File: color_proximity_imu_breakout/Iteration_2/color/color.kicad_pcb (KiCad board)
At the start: 2 copper layers, 15 x 16.5 mm, 10 parts, among them J4 Conn_01x05, U6 ICM-20602

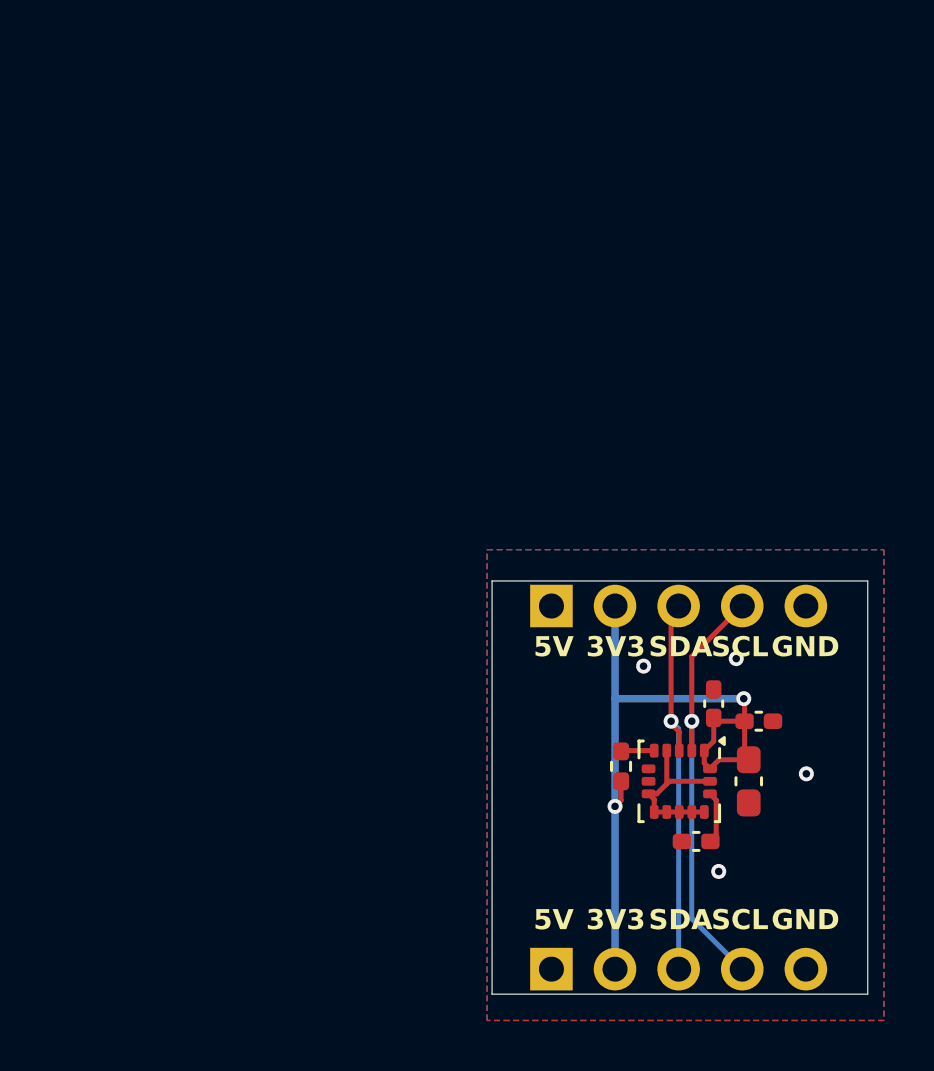
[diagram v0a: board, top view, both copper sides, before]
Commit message: Iteration 2 of color, distance, and imu sensor boards
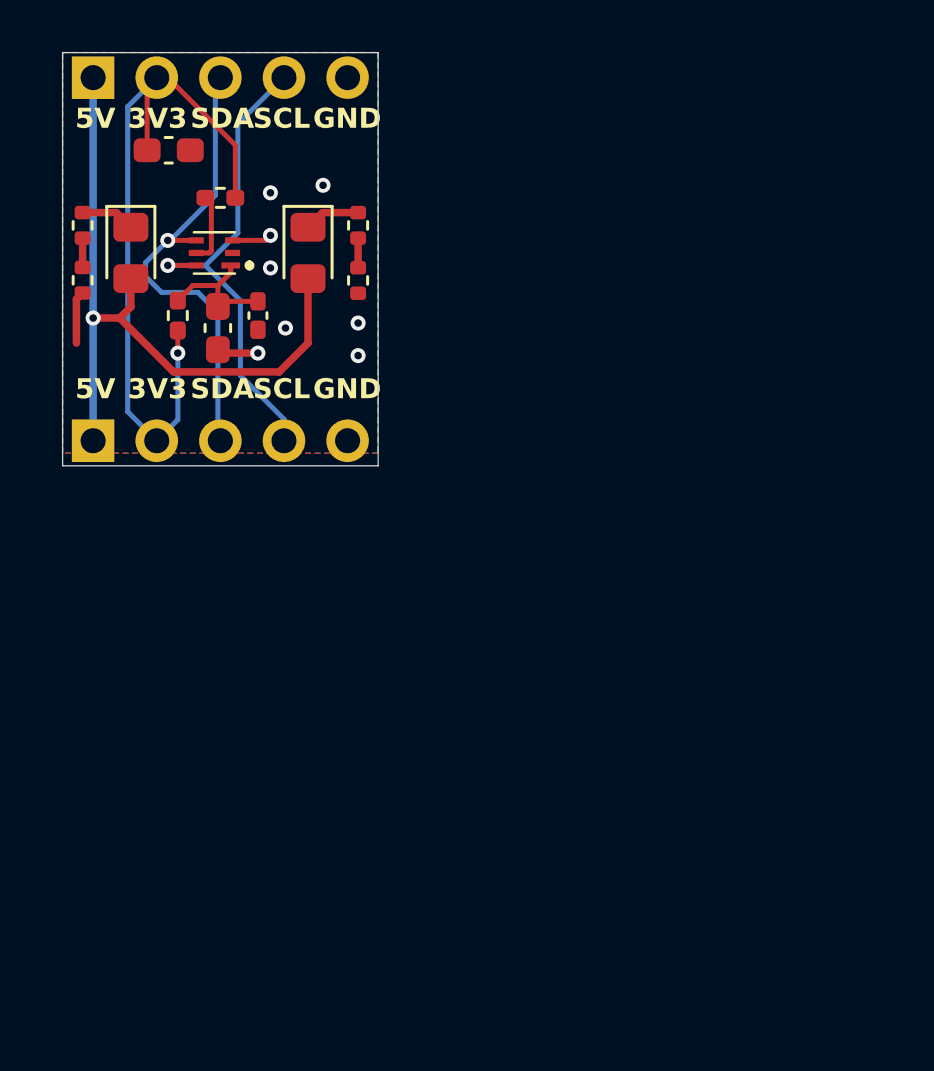
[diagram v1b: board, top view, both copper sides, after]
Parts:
- removed C10, C7: 0.1u, Capacitor_SMD:C_0402_1005Metric_Pad0.74x0.62mm_HandSolder
- removed C8: 2.2u, Capacitor_SMD:C_0603_1608Metric_Pad1.08x0.95mm_HandSolder
- removed C9: 10n, Capacitor_SMD:C_0402_1005Metric_Pad0.74x0.62mm_HandSolder
- removed the G*** at (122.8, 129.5)
- removed the G*** at (124.4, 134.3)
- removed the J4 at (121.4, 140.7)
- removed the J4 at (121.4, 126.2)
- removed R19: 4.7k, Resistor_SMD:R_0402_1005Metric_Pad0.72x0.64mm_HandSolder
- removed U6: ICM-20602, Package_LGA:LGA-16_3x3mm_P0.5mm_LayoutBorder3x5y
- added C14: 10u, Capacitor_SMD:C_0603_1608Metric_Pad1.08x0.95mm_HandSolder, F.Cu at (106.1, 108.0)
- added C4: 1u, Capacitor_SMD:C_0603_1608Metric_Pad1.08x0.95mm_HandSolder, F.Cu at (108.1, 115.1)
- added C5: 0.1u, Capacitor_SMD:C_0402_1005Metric_Pad0.74x0.62mm_HandSolder, F.Cu at (109.7, 114.6)
- added D1: WHITE, LED_SMD:LED_0805_2012Metric_Pad1.15x1.40mm_HandSolder, F.Cu at (111.7, 112.1)
- added D2: WHITE, LED_SMD:LED_0805_2012Metric_Pad1.15x1.40mm_HandSolder, F.Cu at (104.6, 112.1)
- added G***: LOGO, LOGO, B.Cu at (104.5, 108.4)
- added G***: LOGO, LOGO, B.Cu at (105.2, 113.5)
- added IC2: ISL29125IROZ-T7, ISL29125:ISL29125IROZT7, F.Cu at (108.0, 112.1)
- added J4: Conn_01x05, Connector_PinHeader_2.54mm:PinHeader_1x05_P2.54mm_Vertical, F.Cu at (103.1, 105.1)
- added J4: Conn_01x05, Connector_PinHeader_2.54mm:PinHeader_1x05_P2.54mm_Vertical, F.Cu at (103.1, 119.6)
- added R15: 100, Resistor_SMD:R_0402_1005Metric_Pad0.72x0.64mm_HandSolder, F.Cu at (106.5, 114.6)
- added R16: 4.7k, Resistor_SMD:R_0402_1005Metric_Pad0.72x0.64mm_HandSolder, F.Cu at (108.2, 109.9)
- added R17: 120, Resistor_SMD:R_0402_1005Metric, F.Cu at (113.7, 111.0)
- added R18: 120, Resistor_SMD:R_0402_1005Metric, F.Cu at (102.7, 111.0)
- added R30: 120, Resistor_SMD:R_0402_1005Metric, F.Cu at (113.7, 113.2)
- added R32: 120, Resistor_SMD:R_0402_1005Metric, F.Cu at (102.7, 113.2)
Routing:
- net +5V: track 0.02 -> 28.8 mm, vias 0 -> 1
- net Net-(IC2-VDD): track 0.00 -> 5.39 mm
- net Net-(IC2-~{INT}): track 0.00 -> 2.86 mm
- net /sda: track 16.3 -> 19.1 mm
- net Net-(D2-K): track 0.00 -> 2.62 mm
- net Net-(D1-K): track 0.00 -> 2.57 mm
- net /scl: track 17.3 -> 19.7 mm
- net Net-(U6-REGOUT): track 2.10 -> 0.00 mm
- net Net-(U6-~{CS}): track 1.34 -> 0.00 mm
- net GND: track 6.80 -> 5.49 mm, vias 4 -> 8
- net Net-(R17-Pad2): track 0.00 -> 1.18 mm
- net Net-(R18-Pad2): track 0.00 -> 1.17 mm
- net +3.3V: track 29.0 -> 29.6 mm, vias 2 -> 1
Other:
- board size 15 x 16.5 mm -> 12.6 x 16.5 mm

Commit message: Color Board Iteration 2 Updated
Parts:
- removed J4 (x2): Conn_01x05, Connector_PinHeader_2.54mm:PinHeader_1x05_P2.54mm_Vertical
- added C1: 10u, Capacitor_SMD:C_0603_1608Metric_Pad1.08x0.95mm_HandSolder, F.Cu at (107.6, 116.4)
- added G***: LOGO, pcb_footprints:ras, B.Cu at (105.2, 121.6)
- added G***: LOGO, pcb_footprints:vexu_ghost, B.Cu at (112.0, 115.0)
- added J1: Conn_01x10, pcb_footprints:GT-B0502MSV27-10S1101, F.Cu at (111.6, 107.8)
- added J2: Conn_01x10, pcb_footprints:GT-B0502MSV27-10S1101, F.Cu at (105.2, 120.5)
- added REF**: MountingHole_#4_3.175mm, pcb_footprints:MountingHole_#4_3.175mm, F.Cu at (111.6, 120.5)
- added REF**: MountingHole_#4_3.175mm, pcb_footprints:MountingHole_#4_3.175mm, F.Cu at (105.2, 107.8)
- moved R18 12.5 mm to (114.2, 115.7)
- moved R17 12.1 mm to (102.5, 115.5)
- moved R32 11.8 mm to (113.8, 117.2), turned to 180 degrees
- moved R30 11.4 mm to (103.0, 117.0), turned to 0 degrees
- moved D2 8.88 mm to (113.5, 112.5), turned to 90 degrees
- moved D1 8.71 mm to (103.0, 112.5), turned to 90 degrees
- moved C14 5.85 mm to (105.4, 113.8), turned to -90 degrees
- moved R15 5.43 mm to (111.8, 113.2), turned to 90 degrees
- moved R16 3.94 mm to (110.5, 113.1), turned to -90 degrees
- moved G*** 3.82 mm to (104.9, 112.2)
- moved G*** 3.53 mm to (105.6, 117.0)
- moved C5 2.69 mm to (112.0, 116.0)
- moved C4 2.66 mm to (110.5, 116.2)
- moved IC2 1.80 mm to (108.0, 113.9), turned to 0 degrees
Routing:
- net GND: track 5.49 -> 25.9 mm, vias 8 -> 6
- net Net-(IC2-VDD): track 5.39 -> 12.3 mm, vias 0 -> 2
- net +3.3V: track 29.6 -> 34.5 mm, vias 1 -> 2
- net +5V: track 28.8 -> 25.2 mm, vias 1 -> 2
- net /sda: track 19.1 -> 20.3 mm, vias 1 -> 3
- net /scl: track 19.7 -> 18.6 mm, vias 1 -> 2
- net Net-(IC2-~{INT}): track 2.86 -> 1.86 mm
- net Net-(D1-K): track 2.57 -> 1.67 mm
- net Net-(D2-K): track 2.62 -> 2.02 mm
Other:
- board size 12.6 x 16.5 mm -> 13 x 20 mm
- board text added: "Designed By Gengwen Li Trung Le"
- board text added: "Short = increase brightness"
- board text removed: "3V3"
- board text removed: "5V"
- board text removed: "Designed By Gengwen Li"
- board text removed: "GND"
- board text removed: "SCL"
- board text removed: "SDA"

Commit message: color board iteration 2 updated
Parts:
- removed C14: 10u, Capacitor_SMD:C_0603_1608Metric_Pad1.08x0.95mm_HandSolder
- added C2: 10u, Capacitor_SMD:C_0603_1608Metric_Pad1.08x0.95mm_HandSolder, F.Cu at (105.4, 113.6)
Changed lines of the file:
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@@
 			(unlocked yes)
 			(layer "F.SilkS")
+			(hide yes)
 			(effects
 				(font
@@
 		)
 	)
+	(footprint "Capacitor_SMD:C_0603_1608Metric_Pad1.08x0.95mm_HandSolder"
+		(layer "F.Cu")
+		(at 105.4 113.6 90)
+		(descr "Capacitor SMD 0603 (1608 Metric), square (rectangular) end terminal, IPC-7351 nominal with elongated pad for handsoldering. (Body size source: IPC-SM-782 page 76, https://www.pcb-3d.com/wordpress/wp-content/uploads/ipc-sm-782a_amendment_1_and_2.pdf), generated with kicad-footprint-generator")
+		(tags "capacitor handsolder")
+		(property "Reference" "C2"
+			(at 0 -1.43 90)
+			(layer "F.SilkS")
+			(hide yes)
+			(effects
+				(font
+					(size 1 1)
+					(thickness 0.15)
+				)
+			)
+		)
+		(property "Value" "10u"
+			(at 0 1.43 90)
+			(layer "F.Fab")
+			(hide yes)
+			(effects
+				(font
+					(size 1 1)
+					(thickness 0.15)
+				)
+			)
+		)
+		(property "Datasheet" "~"
+			(at 0 0 90)
+			(layer "F.Fab")
+			(hide yes)
+			(effects
+				(font
+					(size 1.27 1.27)
+					(thickness 0.15)
+				)
+			)
+		)
+		(property "Description" "Unpolarized capacitor"
+			(at 0 0 90)
+			(layer "F.Fab")
+			(hide yes)
+			(effects
+				(font
+					(size 1.27 1.27)
+					(thickness 0.15)
+				)
+			)
+		)
+		(property "Supplier Name" "JLCPCB"
+			(at 0 0 90)
+			(unlocked yes)
+			(layer "F.Fab")
+			(hide yes)
+			(effects
+				(font
+					(size 1 1)
+					(thickness 0.15)
+				)
+			)
+		)
+		(property "Supplier Part Number" "C15849"
+			(at 0 0 90)
+			(unlocked yes)
+			(layer "F.Fab")
+			(hide yes)
+			(effects
+				(font
+					(size 1 1)
+					(thickness 0.15)
+				)
+			)
+		)
+		(property "Substitution_Value" ""
+			(at 0 0 90)
+			(unlocked yes)
+			(layer "F.Fab")
+			(hide yes)
+			(effects
+				(font
+					(size 1 1)
+					(thickness 0.15)
+				)
+			)
+		)
+		(property "Variant" ""
+			(at 0 0 90)
+			(unlocked yes)
+			(layer "F.Fab")
+			(hide yes)
+			(effects
+				(font
+					(size 1 1)
+					(thickness 0.15)
+				)
+			)
+		)
+		(property "JLCPCB Part" "C15849"
+			(at 0 0 90)
+			(unlocked yes)
+			(layer "F.Fab")
+			(hide yes)
+			(effects
+				(font
+					(size 1 1)
+					(thickness 0.15)
+				)
+			)
+		)
+		(property ki_fp_filters "C_*")
+		(sheetname "/")
+		(sheetfile "color.kicad_sch")
+		(attr smd)
+		(fp_line
+			(start -0.146267 -0.51)
+			(end 0.146267 -0.51)
+			(stroke
+				(width 0.12)
+				(type solid)
+			)
+			(layer "F.SilkS")
+		)
+		(fp_line
+			(start -0.146267 0.51)
+			(end 0.146267 0.51)
+			(stroke
+				(width 0.12)
+				(type solid)
+			)
+			(layer "F.SilkS")
+		)
+		(fp_poly
+			(pts
+				(xy -1.65 -0.73) (xy 1.65 -0.73) (xy 1.65 0.73) (xy -1.65 0.73)
+			)
+			(stroke
+				(width 0.05)
+				(type solid)
+			)
+			(fill no)
+			(layer "F.CrtYd")
+		)
+		(fp_poly
+			(pts
+				(xy -0.8 -0.4) (xy 0.8 -0.4) (xy 0.8 0.4) (xy -0.8 0.4)
+			)
+			(stroke
+				(width 0.1)
+				(type solid)
+			)
+			(fill no)
+			(layer "F.Fab")
+		)
+		(fp_text user "${REFERENCE}"
+			(at 0 0 90)
+			(layer "F.Fab")
+			(effects
+				(font
+					(size 0.4 0.4)
+					(thickness 0.06)
+				)
+			)
+		)
+		(pad "1" smd roundrect
+			(at -0.862501 0 90)
+			(size 1.075 0.95)
+			(layers "F.Cu" "F.Mask" "F.Paste")
+			(roundrect_rratio 0.25)
+			(net 3 "GND")
+			(pintype "passive")
+		)
+		(pad "2" smd roundrect
+			(at 0.862501 0 90)
+			(size 1.075 0.95)
+			(layers "F.Cu" "F.Mask" "F.Paste")
+			(roundrect_rratio 0.25)
+			(net 1 "+3.3V")
+			(pintype "passive")
+		)
+		(embedded_fonts no)
+		(model "${KICAD9_3DMODEL_DIR}/Capacitor_SMD.3dshapes/C_0603_1608Metric.step"
+			(offset
+				(xyz 0 0 0)
+			)
+			(scale
+				(xyz 1 1 1)
+			)
+			(rotate
+				(xyz 0 0 0)
+			)
+		)
+	)
 	(footprint "pcb_footprints:GT-B0502MSV27-10S1101"
 		(layer "F.Cu")
@@
 		(embedded_fonts no)
 	)
-	(footprint "Capacitor_SMD:C_0603_1608Metric_Pad1.08x0.95mm_HandSolder"
-		(layer "F.Cu")
-		(at 105.4 113.8 -90)
-		(descr "Capacitor SMD 0603 (1608 Metric), square (rectangular) end terminal, IPC-7351 nominal with elongated pad for handsoldering. (Body size source: IPC-SM-782 page 76, https://www.pcb-3d.com/wordpress/wp-content/uploads/ipc-sm-782a_amendment_1_and_2.pdf), generated with kicad-footprint-generator")
-		(tags "capacitor handsolder")
-		(property "Reference" "C14"
-			(at 0 -1.43 90)
-			(layer "F.SilkS")
-			(hide yes)
-			(effects
-				(font
-					(size 1 1)
-					(thickness 0.15)
-				)
-			)
-		)
-		(property "Value" "10u"
-			(at 0 1.43 90)
-			(layer "F.Fab")
-			(hide yes)
-			(effects
-				(font
-					(size 1 1)
-					(thickness 0.15)
-				)
-			)
-		)
-		(property "Datasheet" "~"
-			(at 0 0 90)
-			(layer "F.Fab")
-			(hide yes)
-			(effects
-				(font
-					(size 1.27 1.27)
-					(thickness 0.15)
-				)
-			)
-		)
-		(property "Description" "Unpolarized capacitor"
-			(at 0 0 90)
-			(layer "F.Fab")
-			(hide yes)
-			(effects
-				(font
-					(size 1.27 1.27)
-					(thickness 0.15)
-				)
-			)
-		)
-		(property "Supplier Name" "JLCPCB"
-			(at 0 0 270)
-			(unlocked yes)
-			(layer "F.Fab")
-			(hide yes)
-			(effects
-				(font
-					(size 1 1)
-					(thickness 0.15)
-				)
-			)
-		)
-		(property "Supplier Part Number" "C15849"
-			(at 0 0 270)
-			(unlocked yes)
-			(layer "F.Fab")
-			(hide yes)
-			(effects
-				(font
-					(size 1 1)
-					(thickness 0.15)
-				)
-			)
-		)
-		(property "Substitution_Value" ""
-			(at 0 0 270)
-			(unlocked yes)
-			(layer "F.Fab")
-			(hide yes)
-			(effects
-				(font
-					(size 1 1)
-					(thickness 0.15)
-				)
-			)
-		)
-		(property "Variant" ""
-			(at 0 0 270)
-			(unlocked yes)
-			(layer "F.Fab")
-			(hide yes)
-			(effects
-				(font
-					(size 1 1)
-					(thickness 0.15)
-				)
-			)
-		)
-		(property "JLCPCB Part" "C15849"
-			(at 0 0 270)
-			(unlocked yes)
-			(layer "F.Fab")
-			(hide yes)
-			(effects
-				(font
-					(size 1 1)
-					(thickness 0.15)
-				)
-			)
-		)
-		(property ki_fp_filters "C_*")
-		(sheetname "/")
-		(sheetfile "color.kicad_sch")
-		(attr smd)
-		(fp_line
-			(start -0.146267 0.51)
-			(end 0.146267 0.51)
-			(stroke
-				(width 0.12)
-				(type solid)
-			)
-			(layer "F.SilkS")
-		)
-		(fp_line
-			(start -0.146267 -0.51)
-			(end 0.146267 -0.51)
-			(stroke
-				(width 0.12)
-				(type solid)
-			)
-			(layer "F.SilkS")
-		)
-		(fp_poly
-			(pts
-				(xy -1.65 -0.73) (xy 1.65 -0.73) (xy 1.65 0.73) (xy -1.65 0.73)
-			)
-			(stroke
-				(width 0.05)
-				(type solid)
-			)
-			(fill no)
-			(layer "F.CrtYd")
-		)
-		(fp_poly
-			(pts
-				(xy -0.8 -0.4) (xy 0.8 -0.4) (xy 0.8 0.4) (xy -0.8 0.4)
-			)
-			(stroke
-				(width 0.1)
-				(type solid)
-			)
-			(fill no)
-			(layer "F.Fab")
-		)
-		(fp_text user "${REFERENCE}"
-			(at 0 0 90)
-			(layer "F.Fab")
-			(effects
-				(font
-					(size 0.4 0.4)
-					(thickness 0.06)
-				)
-			)
-		)
-		(pad "1" smd roundrect
-			(at -0.862501 0 270)
-			(size 1.075 0.95)
-			(layers "F.Cu" "F.Mask" "F.Paste")
-			(roundrect_rratio 0.25)
-			(net 1 "+3.3V")
-			(pintype "passive")
-		)
-		(pad "2" smd roundrect
-			(at 0.862501 0 270)
-			(size 1.075 0.95)
-			(layers "F.Cu" "F.Mask" "F.Paste")
-			(roundrect_rratio 0.25)
-			(net 3 "GND")
-			(pintype "passive")
-		)
-		(embedded_fonts no)
-		(model "${KICAD9_3DMODEL_DIR}/Capacitor_SMD.3dshapes/C_0603_1608Metric.step"
-			(offset
-				(xyz 0 0 0)
-			)
-			(scale
-				(xyz 1 1 1)
-			)
-			(rotate
-				(xyz 0 0 0)
-			)
-		)
-	)
 	(footprint "Capacitor_SMD:C_0402_1005Metric_Pad0.74x0.62mm_HandSolder"

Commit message: breakout board iteration 2 updates
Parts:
- removed R30, R32: 120, Resistor_SMD:R_0402_1005Metric
- R17, R18: value 120 -> 60
- moved G*** 7.34 mm to (105.0, 112.8)
- moved G*** 6.52 mm to (111.4, 113.0)
- moved G*** 1.20 mm to (106.8, 117.0)
- moved C5 1.04 mm to (113.0, 115.7)
- moved R17 0.79 mm to (103.0, 116.1)
- moved D1 0.71 mm to (103.1, 113.2)
- moved C4 0.54 mm to (110.8, 115.8), turned to -50 degrees
- moved R18 0.25 mm to (114.0, 115.7)
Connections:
- D1 pad 2: +5V -> +3.3V
- D2 pad 2: +5V -> +3.3V
- J1 pad 10: +5V -> unconnected-(J1-Pin_10-Pad10)
- J2 pad 10: +5V -> unconnected-(J2-Pin_10-Pad10)
- R17 pad 2: Net-(R17-Pad2) -> GND
- R18 pad 2: Net-(R18-Pad2) -> GND
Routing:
- net +5V: track 25.2 -> 0.00 mm, vias 2 -> 0
- net +3.3V: track 34.5 -> 40.1 mm
- net Net-(R18-Pad2): track 1.02 -> 0.00 mm
- net Net-(R17-Pad2): track 0.99 -> 0.00 mm
- net GND: track 25.9 -> 25.1 mm, vias 6 -> 5
- net Net-(IC2-VDD): track 12.3 -> 13.1 mm
- net /sda: track 20.3 -> 19.6 mm
- net /scl: track 18.6 -> 18.1 mm
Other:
- board text removed: "Short = increase brightness"

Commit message: updated production files
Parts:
- removed the G*** at (105.2, 121.6)
- removed the G*** at (111.4, 113.0)
- G***: moved to F.Cu
- J1, J2: moved to B.Cu
- moved G*** 8.91 mm to (111.4, 106.6), turned to 0 degrees
- moved G*** 3.46 mm to (108.3, 113.9), turned to -145 degrees
- turned C1 to 180 degrees
- turned C2 to -90 degrees
- turned J1 to 180 degrees
- turned J2 to 0 degrees
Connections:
- C1 pad 1: GND -> +3.3V
- C1 pad 2: +3.3V -> GND
- C2 pad 1: GND -> +3.3V
- C2 pad 2: +3.3V -> GND
- J1 pad 10: unconnected-(J1-Pin_10-Pad10) -> GND
- J1 pad 6: GND -> unconnected-(J1-Pin_6-Pad6)
- J1 pad 7: /scl -> +3.3V
- J1 pad 9: +3.3V -> /scl
- J2 pad 10: unconnected-(J2-Pin_10-Pad10) -> GND
- J2 pad 6: GND -> unconnected-(J2-Pin_6-Pad6)
- J2 pad 7: /scl -> +3.3V
- J2 pad 9: +3.3V -> /scl
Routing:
- net +3.3V: track 40.1 -> 36.0 mm, vias 2 -> 5
- net GND: track 25.1 -> 23.4 mm, vias 5 -> 2
- net /scl: track 18.1 -> 17.1 mm, vias 2 -> 1
- net /sda: track 19.6 -> 19.1 mm, vias 3 -> 1
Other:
- board text added: "Designed By: Gengwen Li Trung Le"
- board text removed: "Designed By Gengwen Li Trung Le"
